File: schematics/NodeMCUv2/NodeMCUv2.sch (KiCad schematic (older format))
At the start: 2 parts

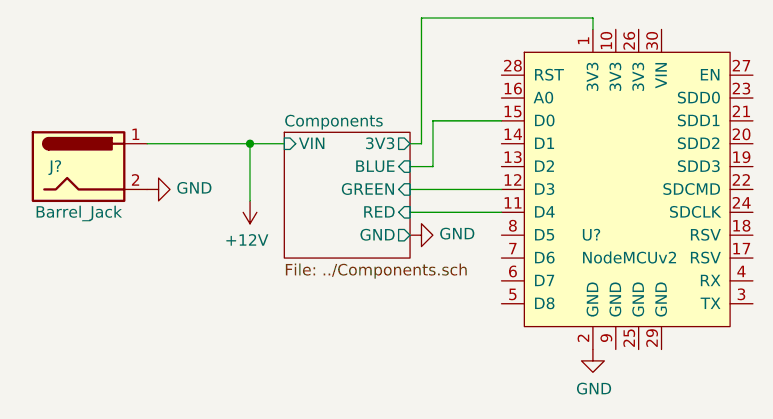
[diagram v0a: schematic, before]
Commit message: Change MOSFET, annotate schematics
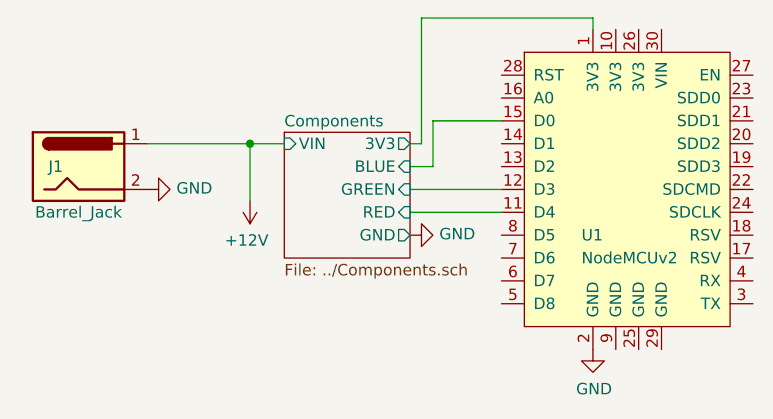
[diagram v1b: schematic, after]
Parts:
- gave numbers to parts that had none: 2
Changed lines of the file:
@@
 $EndSheet
 $Comp
-L power:GND #PWR?
+L power:GND #PWR01
 U 1 1 60F14A50
 P 1650 2650
-F 0 "#PWR?" H 1650 2400 50  0001 C CNN
+F 0 "#PWR01" H 1650 2400 50  0001 C CNN
 F 1 "GND" V 1655 2522 50  0000 R CNN
 F 2 "" H 1650 2650 50  0001 C CNN
@@
 $EndComp
 $Comp
-L Connector:Barrel_Jack J?
+L Connector:Barrel_Jack J1
 U 1 1 60F12523
 P 1350 2550
-F 0 "J?" H 1250 2550 50  0000 C CNN
+F 0 "J1" H 1250 2550 50  0000 C CNN
 F 1 "Barrel_Jack" H 1350 2350 50  0000 C CNN
 F 2 "" H 1400 2510 50  0001 C CNN
@@
 	1650 2450 2100 2450
 $Comp
-L power:+12V #PWR?
+L power:+12V #PWR02
 U 1 1 60F0705D
 P 2100 2700
-F 0 "#PWR?" H 2100 2550 50  0001 C CNN
+F 0 "#PWR02" H 2100 2550 50  0001 C CNN
 F 1 "+12V" H 2115 2873 50  0000 C CNN
 F 2 "" H 2100 2700 50  0001 C CNN
@@
 	2100 2450 2250 2450
 $Comp
-L Custom:NodeMCUv2 U?
+L Custom:NodeMCUv2 U1
 U 1 1 60EFAF8C
 P 3750 2650
-F 0 "U?" H 3550 2450 50  0000 L CNN
+F 0 "U1" H 3550 2450 50  0000 L CNN
 F 1 "NodeMCUv2" H 3550 2350 50  0000 L CNN
 F 2 "" H 3600 1700 50  0001 C CNN
@@
 	3600 1900 3600 1950
 $Comp
-L power:GND #PWR?
+L power:GND #PWR03
 U 1 1 60F0509E
 P 2800 2850
-F 0 "#PWR?" H 2800 2600 50  0001 C CNN
+F 0 "#PWR03" H 2800 2600 50  0001 C CNN
 F 1 "GND" V 2805 2722 50  0000 R CNN
 F 2 "" H 2800 2850 50  0001 C CNN
@@
 $EndComp
 $Comp
-L power:GND #PWR?
+L power:GND #PWR04
 U 1 1 60F057E2
 P 3600 3350
-F 0 "#PWR?" H 3600 3100 50  0001 C CNN
+F 0 "#PWR04" H 3600 3100 50  0001 C CNN
 F 1 "GND" H 3605 3177 50  0000 C CNN
 F 2 "" H 3600 3350 50  0001 C CNN
